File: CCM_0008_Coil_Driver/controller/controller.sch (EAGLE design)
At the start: 203 parts, among them IC1 AD8675, IC10 AD8675, IC11 AD825, IC12 AD825, IC13 AD825, IC14 AD825, IC15 AD825, IC16 AD825, IC17 BUF634U, IC2 AD797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

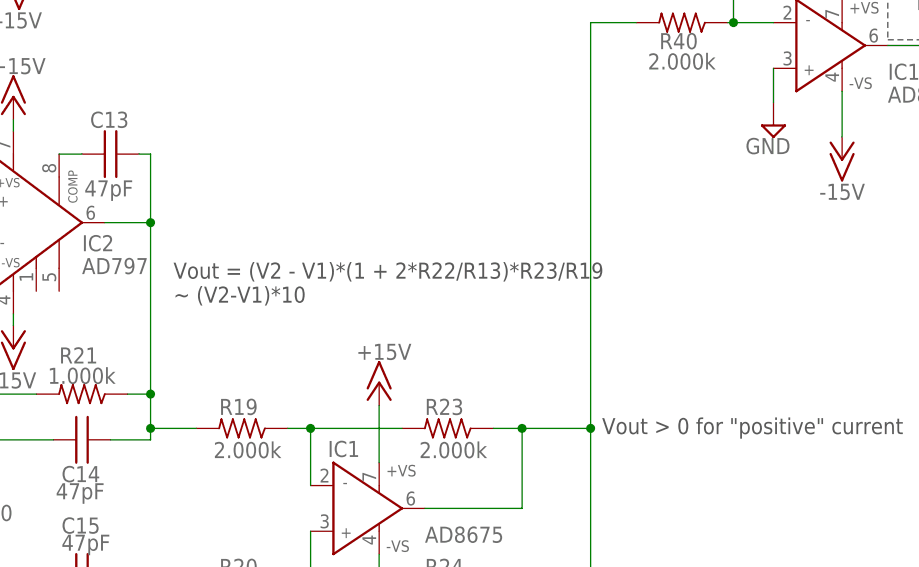
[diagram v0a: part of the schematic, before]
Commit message: started design of hardware TCL
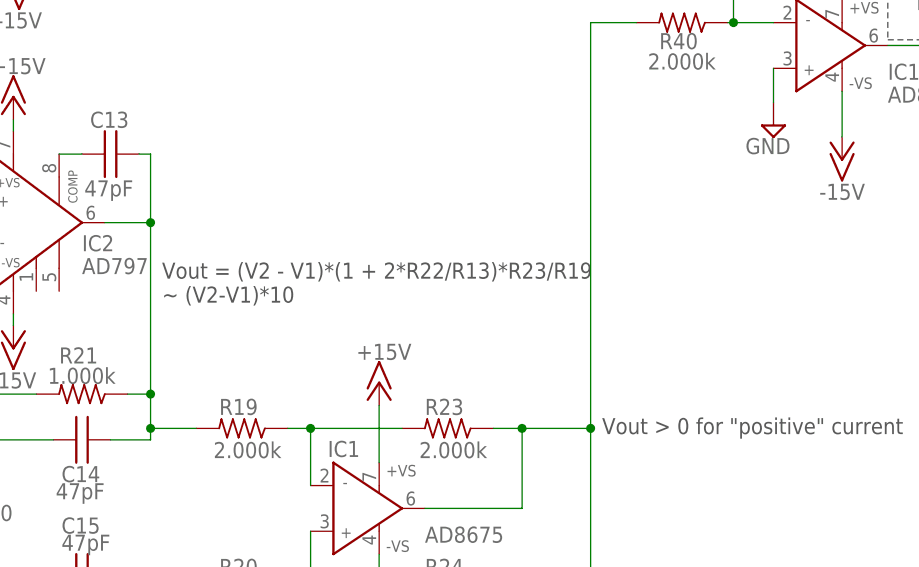
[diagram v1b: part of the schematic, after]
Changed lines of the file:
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@@
 <?xml version="1.0" encoding="utf-8"?>
 <!DOCTYPE eagle SYSTEM "eagle.dtd">
-<eagle version="6.5.0">
+<eagle version="8.3.1">
 <drawing>
 <settings>
 <setting alwaysvectorfont="no"/>
+<setting keepoldvectorfont="yes"/>
 <setting verticaltext="up"/>
 </settings>
@@
 <sheets>
 <sheet>
-<description>P1 Module</description>
+<description>control</description>
 <plain>
 <text x="-494.03" y="135.255" size="1.778" layer="97" rot="R180"></text>
@@
 <text x="23.495" y="27.94" size="1.778" layer="97">V2</text>
 <text x="23.495" y="93.98" size="1.778" layer="97">V1</text>
-<text x="83.185" y="84.455" size="1.778" layer="97">Vout = (V2 - V1)*(1 + 2*R22/R13)*R23/R19
+<text x="81.915" y="84.455" size="1.778" layer="97">Vout = (V2 - V1)*(1 + 2*R22/R13)*R23/R19
 ~ (V2-V1)*10</text>
 <text x="130.81" y="69.85" size="1.778" layer="97">Vout &gt; 0 for "positive" current</text>
